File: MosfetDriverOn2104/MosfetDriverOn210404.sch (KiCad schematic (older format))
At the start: 89 parts, among them J1 I2C HDR, J10 ENCODER HDR, J11 CROSS CONN, J12 motor, J2 AVR-ISP-6, J3 I2C HDR, J4 Screw_Terminal_01x02, J5 I2C HDR, J6 UART HDR, J7 5V HDR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

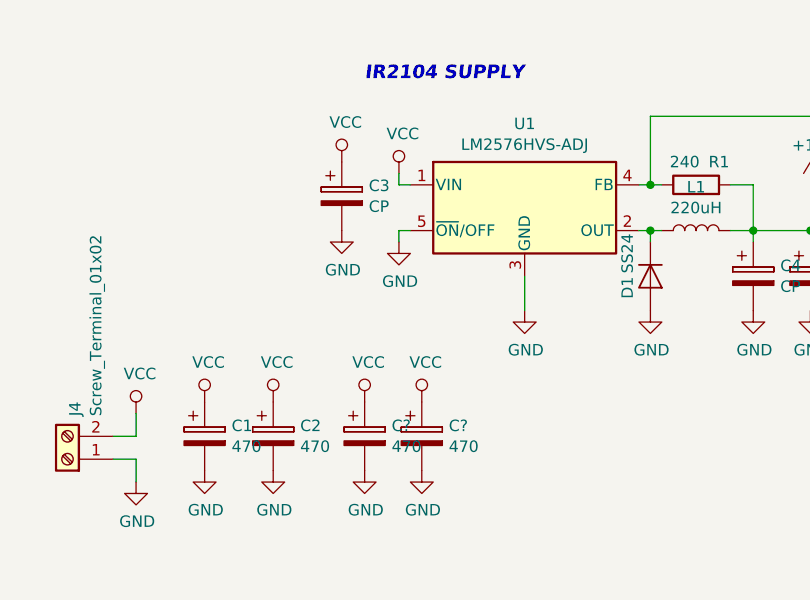
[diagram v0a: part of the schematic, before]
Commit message: Arrenged components,just need to pack a little bit tighter
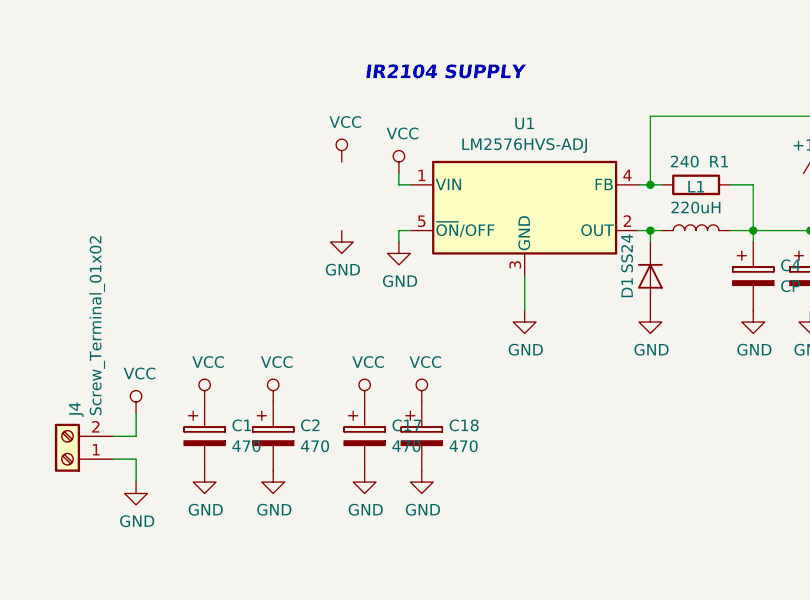
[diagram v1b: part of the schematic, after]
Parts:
- removed C3: CP, Capacitor_SMD:CP_Elec_6.3x5.7, symbol Device:CP
- C8, C9: footprint Capacitor_SMD:CP_Elec_4x4.5 -> Capacitor_SMD:CP_Elec_5x5.3
- gave numbers to parts that had none: 2
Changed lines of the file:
@@
-$EndComp
-$Comp
-L Device:CP C3
-U 1 1 5BD95CE7
-P -7200 2600
-AR Path="/5BD95CE7" Ref="C3"  Part="1"
-AR Path="/5BD0E604/5BD95CE7" Ref="C?"  Part="1"
-F 0 "C3" H -7082 2646 50  0000 L CNN
-F 1 "CP" H -7082 2555 50  0000 L CNN
-F 2 "Capacitor_SMD:CP_Elec_6.3x5.7" H -7162 2450 50  0001 C CNN
-F 3 "~" H -7200 2600 50  0001 C CNN
-	1    -7200 2600
-	1    0    0    -1
 $EndComp
 $Comp
@@
 F 0 "C8" H 5300 -3700 50  0000 L CNN
 F 1 "22u" H 5300 -3800 50  0000 L CNN
-F 2 "Capacitor_SMD:CP_Elec_4x4.5" H 5250 -3750 50  0001 C CNN
+F 2 "Capacitor_SMD:CP_Elec_5x5.3" H 5250 -3750 50  0001 C CNN
 F 3 "~" H 5250 -3750 50  0001 C CNN
 	1    5250 -3750
@@
 F 0 "C9" H 7800 -3700 50  0000 L CNN
 F 1 "22u" H 7800 -3800 50  0000 L CNN
-F 2 "Capacitor_SMD:CP_Elec_4x4.5" H 7750 -3750 50  0001 C CNN
+F 2 "Capacitor_SMD:CP_Elec_5x5.3" H 7750 -3750 50  0001 C CNN
 F 3 "~" H 7750 -3750 50  0001 C CNN
 	1    7750 -3750
@@
 Connection ~ -5150 2750
 $Comp
-L Device:CP C?
+L Device:CP C17
 U 1 1 5C08C5F0
 P -7100 3650
-AR Path="/5C08C5F0" Ref="C?"  Part="1"
+AR Path="/5C08C5F0" Ref="C17"  Part="1"
 AR Path="/5BD0E604/5C08C5F0" Ref="C?"  Part="1"
-F 0 "C?" H -6982 3696 50  0000 L CNN
+F 0 "C17" H -6982 3696 50  0000 L CNN
 F 1 "470" H -6982 3605 50  0000 L CNN
 F 2 "Capacitor_SMD:CP_Elec_10x7.9" H -7062 3500 50  0001 C CNN
@@
 $EndComp
 $Comp
-L Device:CP C?
+L Device:CP C18
 U 1 1 5C08C6BA
 P -6850 3650
-AR Path="/5C08C6BA" Ref="C?"  Part="1"
+AR Path="/5C08C6BA" Ref="C18"  Part="1"
 AR Path="/5BD0E604/5C08C6BA" Ref="C?"  Part="1"
-F 0 "C?" H -6732 3696 50  0000 L CNN
+F 0 "C18" H -6732 3696 50  0000 L CNN
 F 1 "470" H -6732 3605 50  0000 L CNN
 F 2 "Capacitor_SMD:CP_Elec_10x7.9" H -6812 3500 50  0001 C CNN
@@
 AR Path="/5BCF2976/5C08C84C" Ref="#PWR?"  Part="1"
 AR Path="/5BD0E604/5C08C84C" Ref="#PWR?"  Part="1"
-AR Path="/5C08C84C" Ref="#PWR?"  Part="1"
-F 0 "#PWR?" H -7100 3550 50  0001 C CNN
+AR Path="/5C08C84C" Ref="#PWR0178"  Part="1"
+F 0 "#PWR0178" H -7100 3550 50  0001 C CNN
 F 1 "GND" H -7095 3627 50  0000 C CNN
 F 2 "" H -7100 3800 50  0001 C CNN
@@
 AR Path="/5BCF2976/5C08C90D" Ref="#PWR?"  Part="1"
 AR Path="/5BD0E604/5C08C90D" Ref="#PWR?"  Part="1"
-AR Path="/5C08C90D" Ref="#PWR?"  Part="1"
-F 0 "#PWR?" H -6850 3550 50  0001 C CNN
+AR Path="/5C08C90D" Ref="#PWR0179"  Part="1"
+F 0 "#PWR0179" H -6850 3550 50  0001 C CNN
 F 1 "GND" H -6845 3627 50  0000 C CNN
 F 2 "" H -6850 3800 50  0001 C CNN
@@
 AR Path="/5BCF2976/5C08C9CE" Ref="#PWR?"  Part="1"
 AR Path="/5BD0E604/5C08C9CE" Ref="#PWR?"  Part="1"
-AR Path="/5C08C9CE" Ref="#PWR?"  Part="1"
-F 0 "#PWR?" H -7100 3350 50  0001 C CNN
+AR Path="/5C08C9CE" Ref="#PWR0180"  Part="1"
+F 0 "#PWR0180" H -7100 3350 50  0001 C CNN
 F 1 "VCC" H -7083 3673 50  0000 C CNN
 F 2 "" H -7100 3500 50  0001 C CNN
@@
 AR Path="/5BCF2976/5C08CA8F" Ref="#PWR?"  Part="1"
 AR Path="/5BD0E604/5C08CA8F" Ref="#PWR?"  Part="1"
-AR Path="/5C08CA8F" Ref="#PWR?"  Part="1"
-F 0 "#PWR?" H -6850 3350 50  0001 C CNN
+AR Path="/5C08CA8F" Ref="#PWR0181"  Part="1"
+F 0 "#PWR0181" H -6850 3350 50  0001 C CNN
 F 1 "VCC" H -6833 3673 50  0000 C CNN
 F 2 "" H -6850 3500 50  0001 C CNN

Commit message: yet to arrange!
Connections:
- net GND: now also D10.1 (K), D9.1 (K); no longer R17.2, R18.2
- net at U6.7 (XTAL1/PB6): now also R17.1; no longer D9.2 (A)
- net at U6.8 (XTAL2/PB7): now also R18.1; no longer D10.2 (A)
- new net: D9.2 (A), R17.2
- new net: D10.2 (A), R18.2
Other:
- moved on the sheet: D10, D9, R17, R18
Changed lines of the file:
@@
 L Device:LED D?
 U 1 1 5BD9759E
-P 16800 850
+P 16600 850
 AR Path="/5BCF2976/5BD9759E" Ref="D?"  Part="1"
 AR Path="/5BD9759E" Ref="D9"  Part="1"
-F 0 "D9" H 16792 595 50  0000 C CNN
-F 1 "LED" H 16792 686 50  0000 C CNN
-F 2 "LED_SMD:LED_0805_2012Metric" H 16800 850 50  0001 C CNN
-F 3 "~" H 16800 850 50  0001 C CNN
-	1    16800 850
+F 0 "D9" H 16592 595 50  0000 C CNN
+F 1 "LED" H 16592 686 50  0000 C CNN
+F 2 "LED_SMD:LED_0805_2012Metric" H 16600 850 50  0001 C CNN
+F 3 "~" H 16600 850 50  0001 C CNN
+	1    16600 850
 	1    0    0    -1
 $EndComp
@@
 L Device:R_Small R?
 U 1 1 5BD975A5
-P 16450 850
+P 16850 850
 AR Path="/5BCF2976/5BD975A5" Ref="R?"  Part="1"
 AR Path="/5BD975A5" Ref="R17"  Part="1"
-F 0 "R17" H 16350 850 50  0000 C CNN
-F 1 "540" H 16300 950 50  0000 C CNN
-F 2 "Resistor_SMD:R_0805_2012Metric" H 16450 850 50  0001 C CNN
-F 3 "~" H 16450 850 50  0001 C CNN
-	1    16450 850
+F 0 "R17" H 16750 850 50  0000 C CNN
+F 1 "540" H 16700 950 50  0000 C CNN
+F 2 "Resistor_SMD:R_0805_2012Metric" H 16850 850 50  0001 C CNN
+F 3 "~" H 16850 850 50  0001 C CNN
+	1    16850 850
 	0    1    1    0
 $EndComp
@@
 L Device:LED D?
 U 1 1 5BD975B2
-P 16800 1150
+P 16600 1150
 AR Path="/5BCF2976/5BD975B2" Ref="D?"  Part="1"
 AR Path="/5BD975B2" Ref="D10"  Part="1"
-F 0 "D10" H 16792 895 50  0000 C CNN
-F 1 "LED" H 16792 986 50  0000 C CNN
-F 2 "LED_SMD:LED_0805_2012Metric" H 16800 1150 50  0001 C CNN
-F 3 "~" H 16800 1150 50  0001 C CNN
-	1    16800 1150
+F 0 "D10" H 16592 895 50  0000 C CNN
+F 1 "LED" H 16592 986 50  0000 C CNN
+F 2 "LED_SMD:LED_0805_2012Metric" H 16600 1150 50  0001 C CNN
+F 3 "~" H 16600 1150 50  0001 C CNN
+	1    16600 1150
 	1    0    0    -1
 $EndComp
@@
 L Device:R_Small R?
 U 1 1 5BD975B9
-P 16450 1150
+P 16850 1150
 AR Path="/5BCF2976/5BD975B9" Ref="R?"  Part="1"
 AR Path="/5BD975B9" Ref="R18"  Part="1"
-F 0 "R18" H 16350 1150 50  0000 C CNN
-F 1 "540" H 16300 1250 50  0000 C CNN
-F 2 "Resistor_SMD:R_0805_2012Metric" H 16450 1150 50  0001 C CNN
-F 3 "~" H 16450 1150 50  0001 C CNN
-	1    16450 1150
+F 0 "R18" H 16750 1150 50  0000 C CNN
+F 1 "540" H 16700 1250 50  0000 C CNN
+F 2 "Resistor_SMD:R_0805_2012Metric" H 16850 1150 50  0001 C CNN
+F 3 "~" H 16850 1150 50  0001 C CNN
+	1    16850 1150
 	0    1    1    0
 $EndComp
-Wire Wire Line
-	16650 1150 16550 1150
-Wire Wire Line
-	16650 850  16550 850
 Wire Wire Line
 	17050 850  16950 850
@@
 $EndComp
 Wire Wire Line
-	16350 850  16250 850
-Wire Wire Line
 	16250 850  16250 1150
-Wire Wire Line
-	16350 1150 16250 1150
 Connection ~ 16250 1150
 Wire Wire Line
@@
 	1    0    0    -1
 $EndComp
+Wire Wire Line
+	16250 850  16450 850
+Wire Wire Line
+	16250 1150 16450 1150
 $EndSCHEMATC

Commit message: necktie pattern
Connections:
- net +5V: now also J10.2 (Pin_2), J6.2 (Pin_2); no longer J10.4 (Pin_4), J6.4 (Pin_4)
- net A: now also J10.4 (Pin_4); no longer J10.3 (Pin_3)
- net B: now also J10.3 (Pin_3); no longer J10.2 (Pin_2)
- net GND: now also J1.3 (Pin_3), J3.3 (Pin_3), J5.3 (Pin_3); no longer J1.1 (Pin_1), J3.1 (Pin_1), J5.1 (Pin_1)
- net RX: no longer J6.3 (Pin_3)
- net SCL: now also J1.1 (Pin_1), J3.1 (Pin_1), J5.1 (Pin_1); no longer J1.2 (Pin_2), J3.2 (Pin_2), J5.2 (Pin_2)
- net SDA: now also J1.2 (Pin_2), J3.2 (Pin_2), J5.2 (Pin_2); no longer J1.3 (Pin_3), J3.3 (Pin_3), J5.3 (Pin_3)
- net TX: no longer J6.2 (Pin_2)
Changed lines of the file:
@@
 L power:+5V #PWR0118
 U 1 1 5BD95BFB
-P -5900 -550
+P -6100 -350
 AR Path="/5BD95BFB" Ref="#PWR0118"  Part="1"
 AR Path="/5BD0E604/5BD95BFB" Ref="#PWR?"  Part="1"
-F 0 "#PWR0118" H -5900 -700 50  0001 C CNN
-F 1 "+5V" H -5885 -377 50  0000 C CNN
-F 2 "" H -5900 -550 50  0001 C CNN
-F 3 "" H -5900 -550 50  0001 C CNN
-	1    -5900 -550
+F 0 "#PWR0118" H -6100 -500 50  0001 C CNN
+F 1 "+5V" H -6085 -177 50  0000 C CNN
+F 2 "" H -6100 -350 50  0001 C CNN
+F 3 "" H -6100 -350 50  0001 C CNN
+	1    -6100 -350
 	1    0    0    -1
 $EndComp
@@
 L power:GND #PWR0119
 U 1 1 5BD95C01
-P -5900 -250
+P -6000 -250
 AR Path="/5BD95C01" Ref="#PWR0119"  Part="1"
 AR Path="/5BD0E604/5BD95C01" Ref="#PWR?"  Part="1"
-F 0 "#PWR0119" H -5900 -500 50  0001 C CNN
-F 1 "GND" H -5895 -423 50  0000 C CNN
-F 2 "" H -5900 -250 50  0001 C CNN
-F 3 "" H -5900 -250 50  0001 C CNN
-	1    -5900 -250
-	1    0    0    -1
-$EndComp
-Text Label -6050 -450 0    50   ~ 0
+F 0 "#PWR0119" H -6000 -500 50  0001 C CNN
+F 1 "GND" H -5995 -423 50  0000 C CNN
+F 2 "" H -6000 -250 50  0001 C CNN
+F 3 "" H -6000 -250 50  0001 C CNN
+	1    -6000 -250
+	1    0    0    -1
+$EndComp
+Text Label -6000 -550 0    50   ~ 0
 RX
-Text Label -6050 -350 0    50   ~ 0
+Text Label -6000 -450 0    50   ~ 0
 TX
-Wire Wire Line
-	-6050 -450 -5900 -450
-Wire Wire Line
-	-5900 -350 -6050 -350
-$Comp
-L Connector:Conn_01x04_Male J5
-U 1 1 5BD95C0B
-P -7950 -250
-AR Path="/5BD95C0B" Ref="J5"  Part="1"
-AR Path="/5BD0E604/5BD95C0B" Ref="J?"  Part="1"
-F 0 "J5" H -7978 -370 50  0000 R CNN
-F 1 "I2C HDR" H -7800 -550 50  0000 R CNN
-F 2 "Connector_PinHeader_2.54mm:PinHeader_1x04_P2.54mm_Vertical" H -7950 -250 50  0001 C CNN
-F 3 "~" H -7950 -250 50  0001 C CNN
-	1    -7950 -250
-	-1   0    0    1
-$EndComp
-$Comp
-L power:+5V #PWR0120
-U 1 1 5BD95C12
-P -8150 -450
-AR Path="/5BD95C12" Ref="#PWR0120"  Part="1"
-AR Path="/5BD0E604/5BD95C12" Ref="#PWR?"  Part="1"
-F 0 "#PWR0120" H -8150 -600 50  0001 C CNN
-F 1 "+5V" H -8135 -277 50  0000 C CNN
-F 2 "" H -8150 -450 50  0001 C CNN
-F 3 "" H -8150 -450 50  0001 C CNN
-	1    -8150 -450
-	1    0    0    -1
-$EndComp
-$Comp
-L power:GND #PWR0121
-U 1 1 5BD95C18
-P -8150 -150
-AR Path="/5BD95C18" Ref="#PWR0121"  Part="1"
-AR Path="/5BD0E604/5BD95C18" Ref="#PWR?"  Part="1"
-F 0 "#PWR0121" H -8150 -400 50  0001 C CNN
-F 1 "GND" H -8145 -323 50  0000 C CNN
-F 2 "" H -8150 -150 50  0001 C CNN
-F 3 "" H -8150 -150 50  0001 C CNN
-	1    -8150 -150
-	1    0    0    -1
-$EndComp
-Text Label -8300 -350 0    50   ~ 0
-SDA
-Text Label -8300 -250 0    50   ~ 0
-SCL
-Wire Wire Line
-	-8150 -350 -8300 -350
-Wire Wire Line
-	-8300 -250 -8150 -250
 $Comp
 L Connector:Conn_01x04_Male J8
@@
 $EndComp
 $Comp
-L Connector:Conn_01x04_Male J1
-U 1 1 5BD95C64
-P -9000 -250
-AR Path="/5BD95C64" Ref="J1"  Part="1"
-AR Path="/5BD0E604/5BD95C64" Ref="J?"  Part="1"
-F 0 "J1" H -9028 -370 50  0000 R CNN
-F 1 "I2C HDR" H -8850 -550 50  0000 R CNN
-F 2 "Connector_PinHeader_2.54mm:PinHeader_1x04_P2.54mm_Vertical" H -9000 -250 50  0001 C CNN
-F 3 "~" H -9000 -250 50  0001 C CNN
-	1    -9000 -250
-	-1   0    0    1
-$EndComp
-$Comp
-L power:+5V #PWR0125
-U 1 1 5BD95C6B
-P -9200 -450
-AR Path="/5BD95C6B" Ref="#PWR0125"  Part="1"
-AR Path="/5BD0E604/5BD95C6B" Ref="#PWR?"  Part="1"
-F 0 "#PWR0125" H -9200 -600 50  0001 C CNN
-F 1 "+5V" H -9185 -277 50  0000 C CNN
-F 2 "" H -9200 -450 50  0001 C CNN
-F 3 "" H -9200 -450 50  0001 C CNN
-	1    -9200 -450
-	1    0    0    -1
-$EndComp
-$Comp
-L power:GND #PWR0126
-U 1 1 5BD95C71
-P -9200 -150
-AR Path="/5BD95C71" Ref="#PWR0126"  Part="1"
-AR Path="/5BD0E604/5BD95C71" Ref="#PWR?"  Part="1"
-F 0 "#PWR0126" H -9200 -400 50  0001 C CNN
-F 1 "GND" H -9195 -323 50  0000 C CNN
-F 2 "" H -9200 -150 50  0001 C CNN
-F 3 "" H -9200 -150 50  0001 C CNN
-	1    -9200 -150
-	1    0    0    -1
-$EndComp
-Text Label -9350 -350 0    50   ~ 0
-SDA
-Text Label -9350 -250 0    50   ~ 0
-SCL
-Wire Wire Line
-	-9200 -350 -9350 -350
-Wire Wire Line
-	-9350 -250 -9200 -250
-$Comp
 L Connector:Conn_01x04_Male J3
 U 1 1 5BD95C7B
@@
 L power:GND #PWR0128
 U 1 1 5BD95C88
-P -8650 -150
+P -8850 -350
 AR Path="/5BD95C88" Ref="#PWR0128"  Part="1"
 AR Path="/5BD0E604/5BD95C88" Ref="#PWR?"  Part="1"
-F 0 "#PWR0128" H -8650 -400 50  0001 C CNN
-F 1 "GND" H -8645 -323 50  0000 C CNN
-F 2 "" H -8650 -150 50  0001 C CNN
-F 3 "" H -8650 -150 50  0001 C CNN
-	1    -8650 -150
-	1    0    0    -1
-$EndComp
-Text Label -8800 -350 0    50   ~ 0
+F 0 "#PWR0128" H -8850 -600 50  0001 C CNN
+F 1 "GND" H -8845 -523 50  0000 C CNN
+F 2 "" H -8850 -350 50  0001 C CNN
+F 3 "" H -8850 -350 50  0001 C CNN
+	1    -8850 -350
+	1    0    0    -1
+$EndComp
+Text Label -8800 -250 0    50   ~ 0
 SDA
-Text Label -8800 -250 0    50   ~ 0
+Text Label -8800 -150 0    50   ~ 0
 SCL
-Wire Wire Line
-	-8650 -350 -8800 -350
 Wire Wire Line
 	-8800 -250 -8650 -250
@@
 L power:+5V #PWR0129
 U 1 1 5BD95C9C
-P -1650 600
+P -1800 800
 AR Path="/5BD95C9C" Ref="#PWR0129"  Part="1"
 AR Path="/5BD0E604/5BD95C9C" Ref="#PWR?"  Part="1"
-F 0 "#PWR0129" H -1650 450 50  0001 C CNN
-F 1 "+5V" H -1635 773 50  0000 C CNN
-F 2 "" H -1650 600 50  0001 C CNN
-F 3 "" H -1650 600 50  0001 C CNN
-	1    -1650 600
+F 0 "#PWR0129" H -1800 650 50  0001 C CNN
+F 1 "+5V" H -1785 973 50  0000 C CNN
+F 2 "" H -1800 800 50  0001 C CNN
+F 3 "" H -1800 800 50  0001 C CNN
+	1    -1800 800
 	1    0    0    -1
 $EndComp
@@
 L power:GND #PWR0130
 U 1 1 5BD95CA2
-P -1650 900
+P -1700 900
 AR Path="/5BD95CA2" Ref="#PWR0130"  Part="1"
 AR Path="/5BD0E604/5BD95CA2" Ref="#PWR?"  Part="1"
-F 0 "#PWR0130" H -1650 650 50  0001 C CNN
-F 1 "GND" H -1645 727 50  0000 C CNN
-F 2 "" H -1650 900 50  0001 C CNN
-F 3 "" H -1650 900 50  0001 C CNN
-	1    -1650 900
-	1    0    0    -1
-$EndComp
-Wire Wire Line
-	-1650 700  -1800 700
+F 0 "#PWR0130" H -1700 650 50  0001 C CNN
+F 1 "GND" H -1695 727 50  0000 C CNN
+F 2 "" H -1700 900 50  0001 C CNN
+F 3 "" H -1700 900 50  0001 C CNN
+	1    -1700 900
+	1    0    0    -1
+$EndComp
 Wire Wire Line
 	-1800 800  -1650 800
-Text Label -1800 700  0    59   Italic 12
+Text Label -1750 600  0    59   Italic 12
 A
-Text Label -1800 800  0    59   Italic 12
+Text Label -1750 700  0    59   Italic 12
 B
 $Comp
@@
 Wire Wire Line
 	16250 1150 16450 1150
+Wire Wire Line
+	-6100 -350 -5900 -350
+Wire Wire Line
+	-5900 -250 -6000 -250
+Wire Wire Line
+	-1750 600  -1650 600
+Wire Wire Line
+	-1750 700  -1650 700
+Wire Wire Line
+	-1650 900  -1700 900
+Wire Wire Line
+	-8800 -150 -8650 -150
+Wire Wire Line
+	-8850 -350 -8650 -350
+$Comp
+L Connector:Conn_01x04_Male J5
+U 1 1 5BFA199C
+P -7850 -250
+AR Path="/5BFA199C" Ref="J5"  Part="1"
+AR Path="/5BD0E604/5BFA199C" Ref="J?"  Part="1"
+F 0 "J5" H -7878 -370 50  0000 R CNN
+F 1 "I2C HDR" H -7700 -550 50  0000 R CNN
+F 2 "Connector_PinHeader_2.54mm:PinHeader_1x04_P2.54mm_Vertical" H -7850 -250 50  0001 C CNN
+F 3 "~" H -7850 -250 50  0001 C CNN
+	1    -7850 -250
+	-1   0    0    1
+$EndComp
+$Comp
+L power:+5V #PWR0120
+U 1 1 5BFA19A3
+P -8050 -450
+AR Path="/5BFA19A3" Ref="#PWR0120"  Part="1"
+AR Path="/5BD0E604/5BFA19A3" Ref="#PWR?"  Part="1"
+F 0 "#PWR0120" H -8050 -600 50  0001 C CNN
+F 1 "+5V" H -8035 -277 50  0000 C CNN
+F 2 "" H -8050 -450 50  0001 C CNN
+F 3 "" H -8050 -450 50  0001 C CNN
+	1    -8050 -450
+	1    0    0    -1
+$EndComp
+$Comp
+L power:GND #PWR0121
+U 1 1 5BFA19A9
+P -8250 -350
+AR Path="/5BFA19A9" Ref="#PWR0121"  Part="1"
+AR Path="/5BD0E604/5BFA19A9" Ref="#PWR?"  Part="1"
+F 0 "#PWR0121" H -8250 -600 50  0001 C CNN
+F 1 "GND" H -8245 -523 50  0000 C CNN
+F 2 "" H -8250 -350 50  0001 C CNN
+F 3 "" H -8250 -350 50  0001 C CNN
+	1    -8250 -350
+	1    0    0    -1
+$EndComp
+Text Label -8200 -250 0    50   ~ 0
+SDA
+Text Label -8200 -150 0    50   ~ 0
+SCL
+Wire Wire Line
+	-8200 -250 -8050 -250
+Wire Wire Line
+	-8200 -150 -8050 -150
+Wire Wire Line
+	-8250 -350 -8050 -350
+$Comp
+L Connector:Conn_01x04_Male J1
+U 1 1 5BFB80C0
+P -9100 -250
+AR Path="/5BFB80C0" Ref="J1"  Part="1"
+AR Path="/5BD0E604/5BFB80C0" Ref="J?"  Part="1"
+F 0 "J1" H -9128 -370 50  0000 R CNN
+F 1 "I2C HDR" H -8950 -550 50  0000 R CNN
+F 2 "Connector_PinHeader_2.54mm:PinHeader_1x04_P2.54mm_Vertical" H -9100 -250 50  0001 C CNN
+F 3 "~" H -9100 -250 50  0001 C CNN
+	1    -9100 -250
+	-1   0    0    1
+$EndComp
+$Comp
+L power:+5V #PWR0125
+U 1 1 5BFB80C7
+P -9300 -450
+AR Path="/5BFB80C7" Ref="#PWR0125"  Part="1"
+AR Path="/5BD0E604/5BFB80C7" Ref="#PWR?"  Part="1"
+F 0 "#PWR0125" H -9300 -600 50  0001 C CNN
+F 1 "+5V" H -9285 -277 50  0000 C CNN
+F 2 "" H -9300 -450 50  0001 C CNN
+F 3 "" H -9300 -450 50  0001 C CNN
+	1    -9300 -450
+	1    0    0    -1
+$EndComp
+$Comp
+L power:GND #PWR0126
+U 1 1 5BFB80CD
+P -9500 -350
+AR Path="/5BFB80CD" Ref="#PWR0126"  Part="1"
+AR Path="/5BD0E604/5BFB80CD" Ref="#PWR?"  Part="1"
+F 0 "#PWR0126" H -9500 -600 50  0001 C CNN
+F 1 "GND" H -9495 -523 50  0000 C CNN
+F 2 "" H -9500 -350 50  0001 C CNN
+F 3 "" H -9500 -350 50  0001 C CNN
+	1    -9500 -350
+	1    0    0    -1
+$EndComp
+Text Label -9450 -250 0    50   ~ 0
+SDA
+Text Label -9450 -150 0    50   ~ 0
+SCL
+Wire Wire Line
+	-9450 -250 -9300 -250
+Wire Wire Line
+	-9450 -150 -9300 -150
+Wire Wire Line
+	-9500 -350 -9300 -350
 $EndSCHEMATC

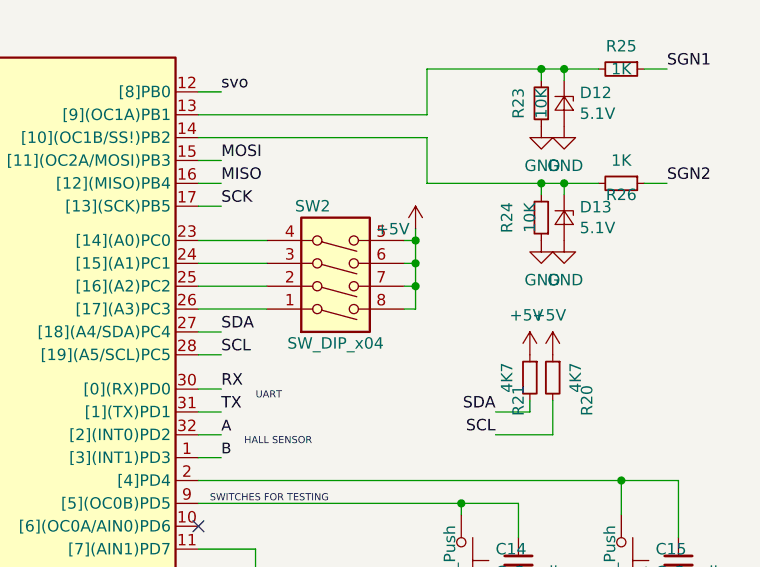
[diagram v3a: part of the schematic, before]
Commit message: add model for mosfet
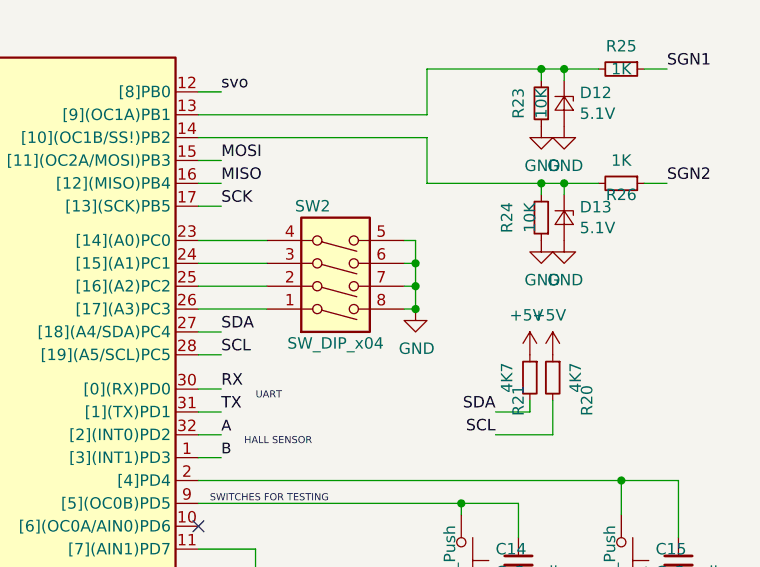
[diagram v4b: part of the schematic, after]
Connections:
- net +5V: no longer SW2.5, SW2.6, SW2.7, SW2.8
- net GND: now also SW2.5, SW2.6, SW2.7, SW2.8
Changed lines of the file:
@@
-$EndComp
-$Comp
-L power:+5V #PWR?
-U 1 1 5BD97570
-P 19400 150
-AR Path="/5BCF2976/5BD97570" Ref="#PWR?"  Part="1"
-AR Path="/5BD97570" Ref="#PWR0147"  Part="1"
-F 0 "#PWR0147" H 19400 0   50  0001 C CNN
-F 1 "+5V" H 19300 150 50  0000 C CNN
-F 2 "" H 19400 150 50  0001 C CNN
-F 3 "" H 19400 150 50  0001 C CNN
-	1    19400 150
-	1    0    0    -1
 $EndComp
 $Comp
@@
 Wire Wire Line
 	18550 50   18450 50
-Wire Wire Line
-	19400 150  19400 200
 Text Label 19500 2300 2    50   ~ 0
 ~SD
@@
 Connection ~ 20300 1250
 Wire Wire Line
-	19350 200  19400 200
-Wire Wire Line
-	19400 200  19400 300
-Wire Wire Line
 	19400 500  19350 500
-Connection ~ 19400 200
 Wire Wire Line
 	19350 400  19400 400
-Connection ~ 19400 400
-Wire Wire Line
-	19400 400  19400 500
 Wire Wire Line
 	19400 300  19350 300
-Connection ~ 19400 300
-Wire Wire Line
-	19400 300  19400 400
 Wire Wire Line
 	18450 200  18750 200
@@
 Wire Wire Line
 	-9500 -350 -9300 -350
+$Comp
+L power:GND #PWR?
+U 1 1 5BDA78C6
+P 19400 500
+AR Path="/5BCF2976/5BDA78C6" Ref="#PWR?"  Part="1"
+AR Path="/5BDA78C6" Ref="#PWR?"  Part="1"
+F 0 "#PWR?" H 19400 250 50  0001 C CNN
+F 1 "GND" H 19405 327 50  0000 C CNN
+F 2 "" H 19400 500 50  0001 C CNN
+F 3 "" H 19400 500 50  0001 C CNN
+	1    19400 500
+	1    0    0    -1
+$EndComp
+Wire Wire Line
+	19400 500  19400 400
+Connection ~ 19400 500
+Wire Wire Line
+	19400 300  19400 400
+Connection ~ 19400 400
+Wire Wire Line
+	19350 200  19400 200
+Wire Wire Line
+	19400 200  19400 300
+Connection ~ 19400 300
 $EndSCHEMATC
